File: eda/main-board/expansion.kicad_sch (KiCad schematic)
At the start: 15 parts, among them J2 Expansion, U11 74HCT541, U17 74HCT541, U18 74HCT245, U5 74HCT138

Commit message: Normalize cap size
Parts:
- C3: footprint Capacitor_THT:C_Disc_D6.0mm_W2.5mm_P5.00mm -> Capacitor_THT:C_Disc_D3.8mm_W2.6mm_P2.50mm
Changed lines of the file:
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@@
       (effects (font (size 1.27 1.27)) (justify left))
     )
-    (property "Footprint" "Capacitor_THT:C_Disc_D6.0mm_W2.5mm_P5.00mm" (at 194.0052 153.67 0)
+    (property "Footprint" "Capacitor_THT:C_Disc_D3.8mm_W2.6mm_P2.50mm" (at 194.0052 153.67 0)
       (effects (font (size 1.27 1.27)) hide)
     )
@@
       (effects (font (size 1.27 1.27)) (justify left))
     )
-    (property "Footprint" "Capacitor_THT:C_Disc_D6.0mm_W2.5mm_P5.00mm" (at 224.4852 153.67 0)
+    (property "Footprint" "Capacitor_THT:C_Disc_D3.8mm_W2.6mm_P2.50mm" (at 224.4852 153.67 0)
       (effects (font (size 1.27 1.27)) hide)
     )
@@
       (effects (font (size 1.27 1.27)) (justify left))
     )
-    (property "Footprint" "Capacitor_THT:C_Disc_D6.0mm_W2.5mm_P5.00mm" (at 234.6452 153.67 0)
+    (property "Footprint" "Capacitor_THT:C_Disc_D3.8mm_W2.6mm_P2.50mm" (at 234.6452 153.67 0)
       (effects (font (size 1.27 1.27)) hide)
     )
@@
       (effects (font (size 1.27 1.27)) (justify left))
     )
-    (property "Footprint" "Capacitor_THT:C_Disc_D6.0mm_W2.5mm_P5.00mm" (at 214.3252 153.67 0)
+    (property "Footprint" "Capacitor_THT:C_Disc_D3.8mm_W2.6mm_P2.50mm" (at 214.3252 153.67 0)
       (effects (font (size 1.27 1.27)) hide)
     )
@@
       (effects (font (size 1.27 1.27)) (justify left))
     )
-    (property "Footprint" "Capacitor_THT:C_Disc_D6.0mm_W2.5mm_P5.00mm" (at 204.1652 153.67 0)
-      (effects (font (size 1.27 1.27)) hide)
-    )
+    (property "Footprint" "Capacitor_THT:C_Disc_D3.8mm_W2.6mm_P2.50mm" (at 204.1652 153.67 0)
+      (effects (font (size 1.27 1.27)) hide)
+    )

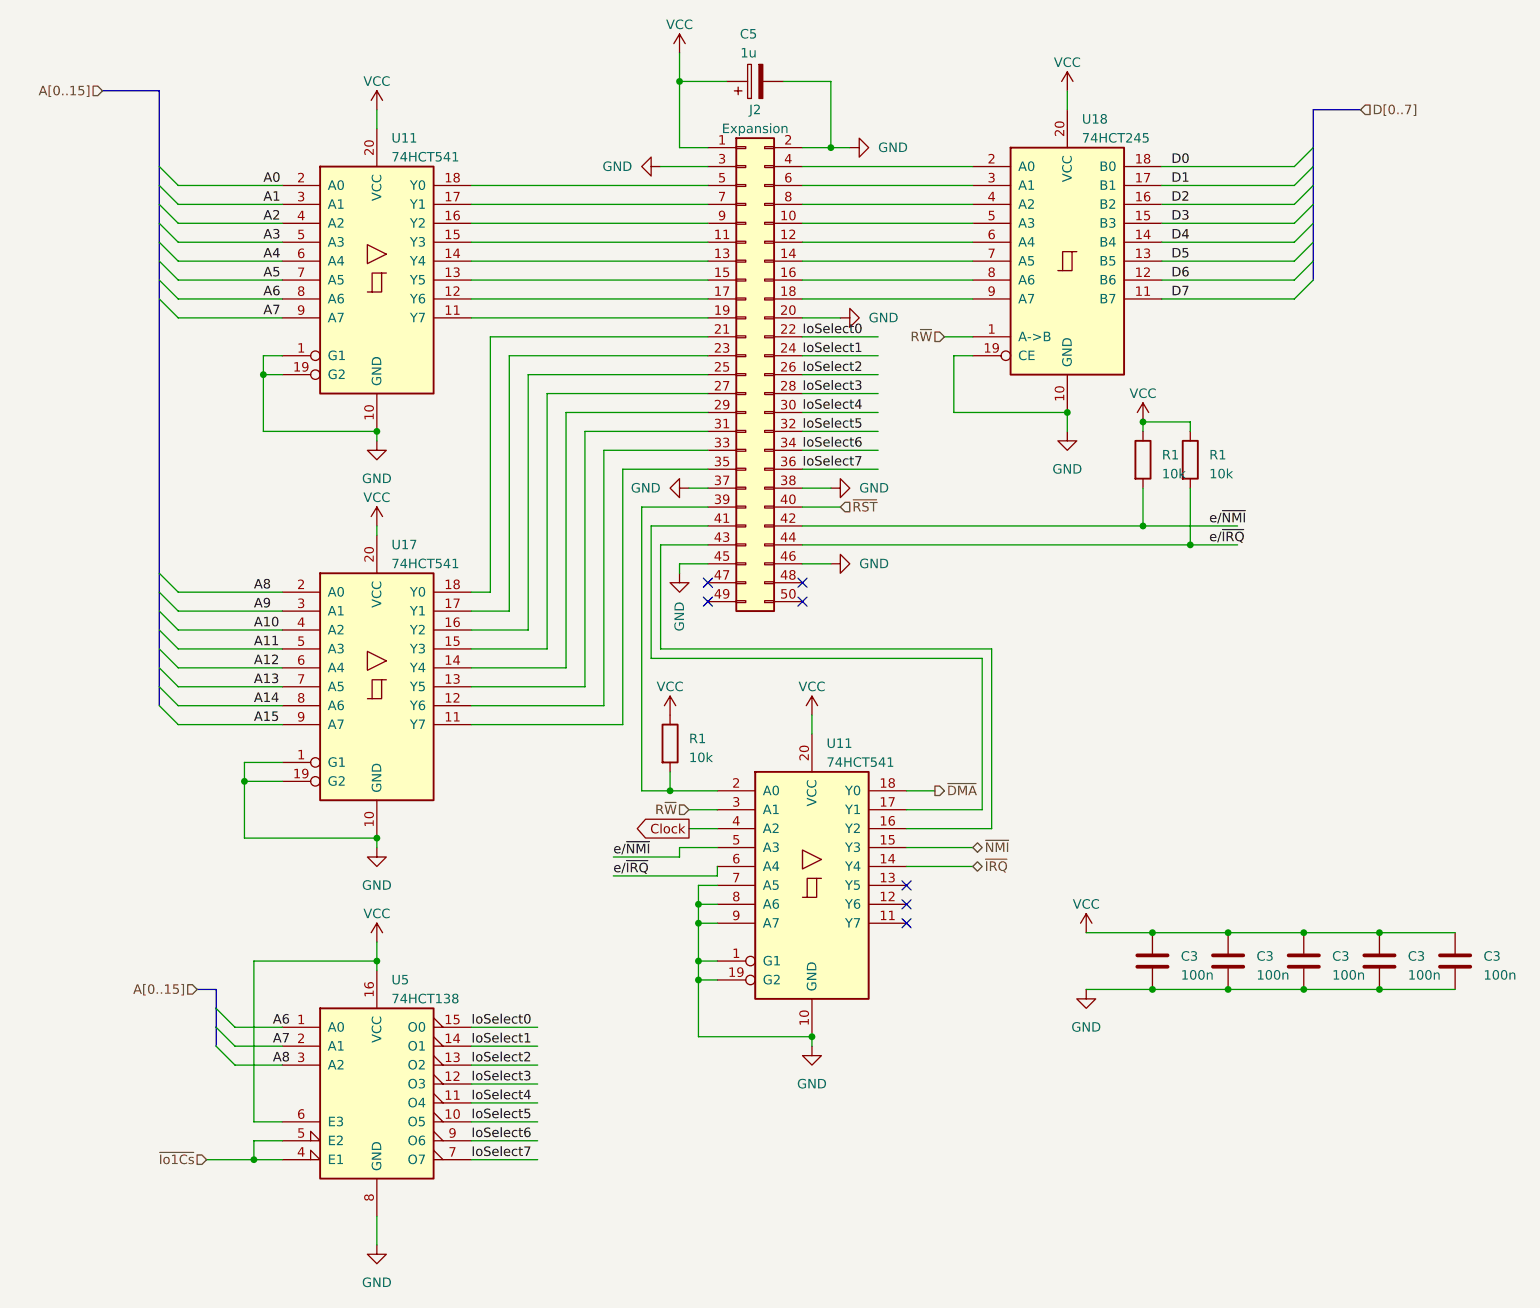
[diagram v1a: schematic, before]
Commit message: Rerouting IO card
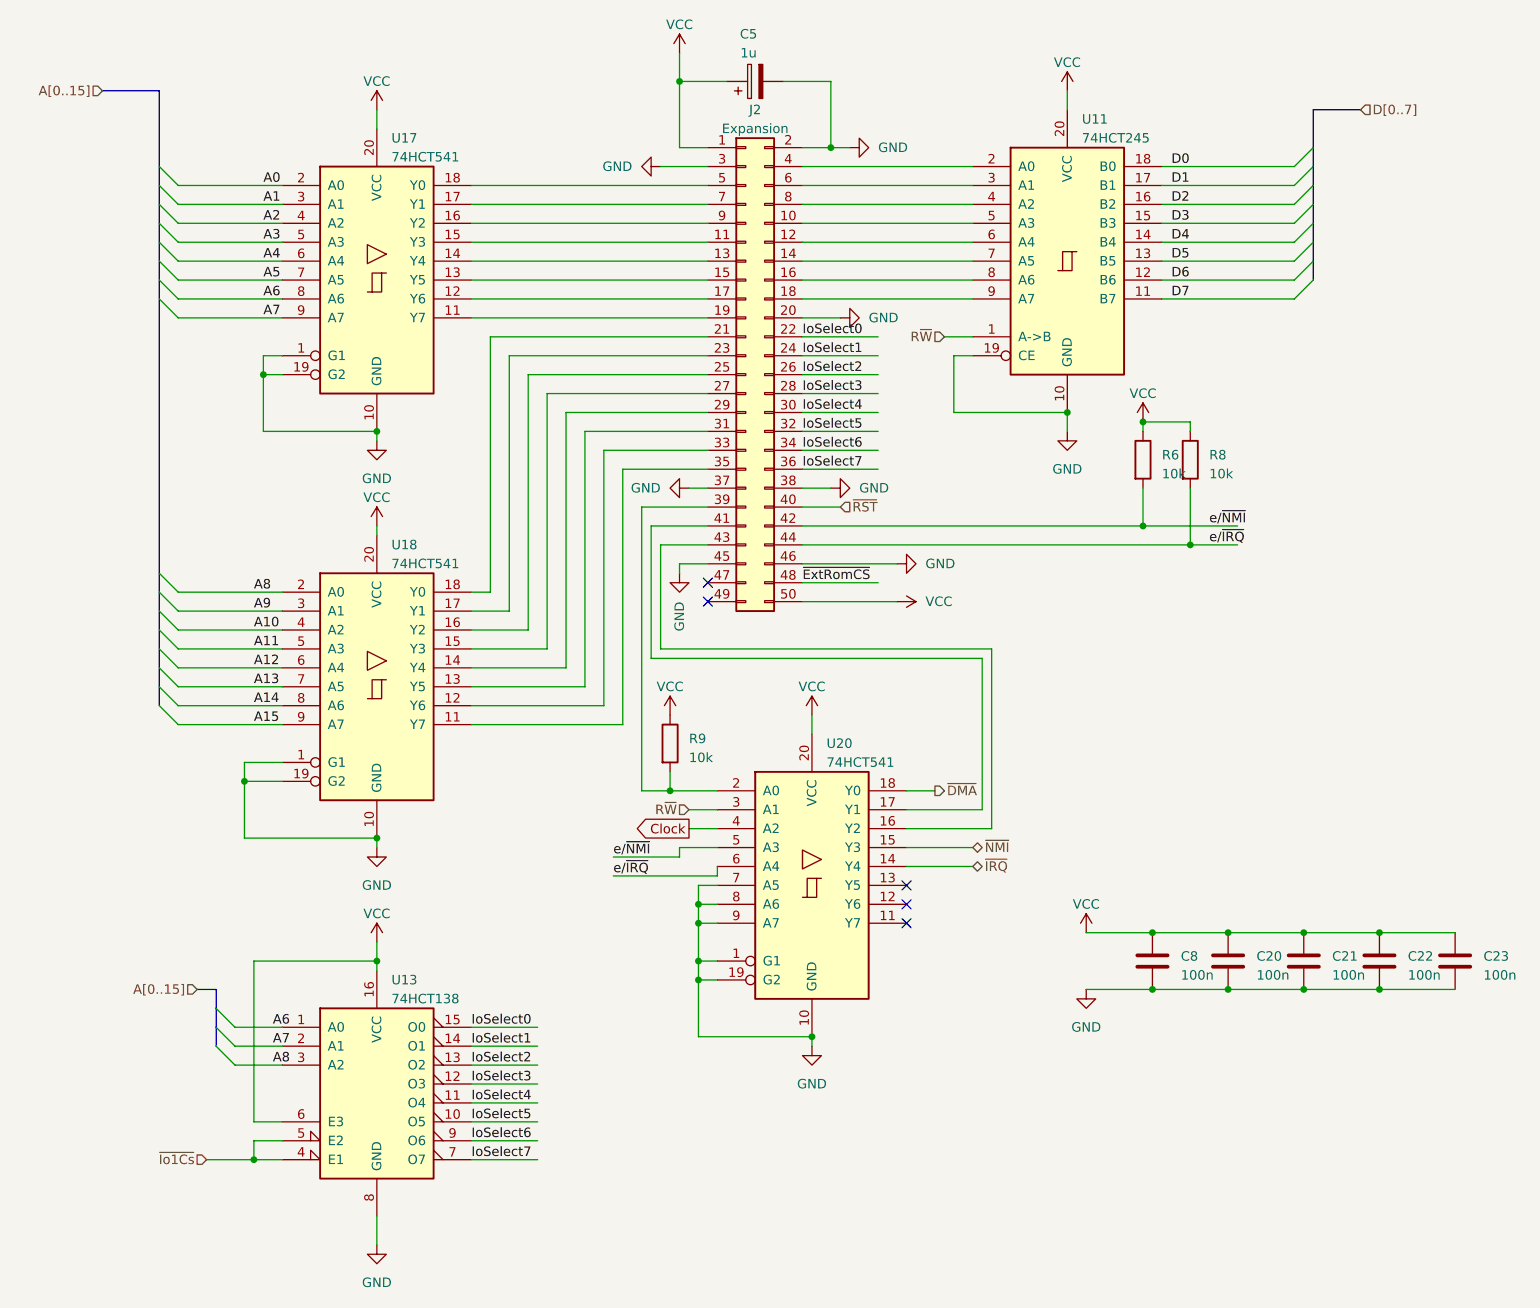
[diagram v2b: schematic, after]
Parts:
- renumbered C3 to C20, C3 to C21, C3 to C22, C3 to C23, C3 to C8, R1 to R6, R1 to R8, R1 to R9, U18 to U11, U5 to U13, U11 to U17, U17 to U18, U11 to U20
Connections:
- net VCC: now also J2.50 (Pin_50)
- net ~{ExtRomCS}: now reaches J2.48 (Pin_48)
- no-connect marks 7 -> 5
